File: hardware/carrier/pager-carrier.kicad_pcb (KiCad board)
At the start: 2 copper layers, 46.2 x 51 mm, 80 parts, among them J1 PANEL, J2 CARDKB, J3 HAPTIC, J4 EXT_LED, J5 PIEZ, J6 USB4235, J7 BATTERY, J8 FRONTLIGHT, M1 Walter, Q1 UMH3N, Q2 SI1308EDL, Q3 MMST3904, Q4 AO3401A, SW1 KMR221GLFS, SW2 JS102011SAQN, U1 CP2102N-A02-GQFN24, U2 SN74LVC2G126DCUR, U3 DRV2605LDGSR, U4 LIS2DW12TR, U5 BQ25185DLHR, U6 MAX17048G+T10, U7 TPS62840DLCR

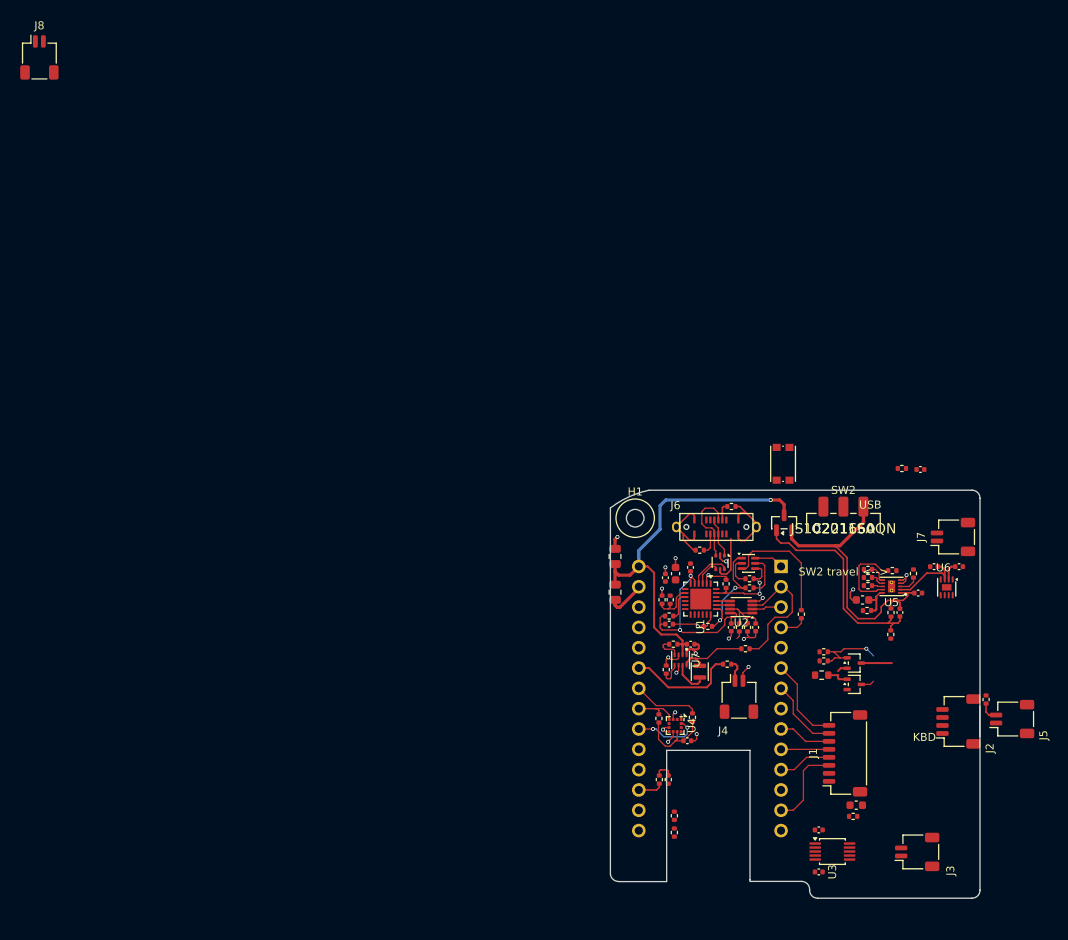
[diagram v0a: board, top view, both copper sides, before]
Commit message: Hand routed the carrier board
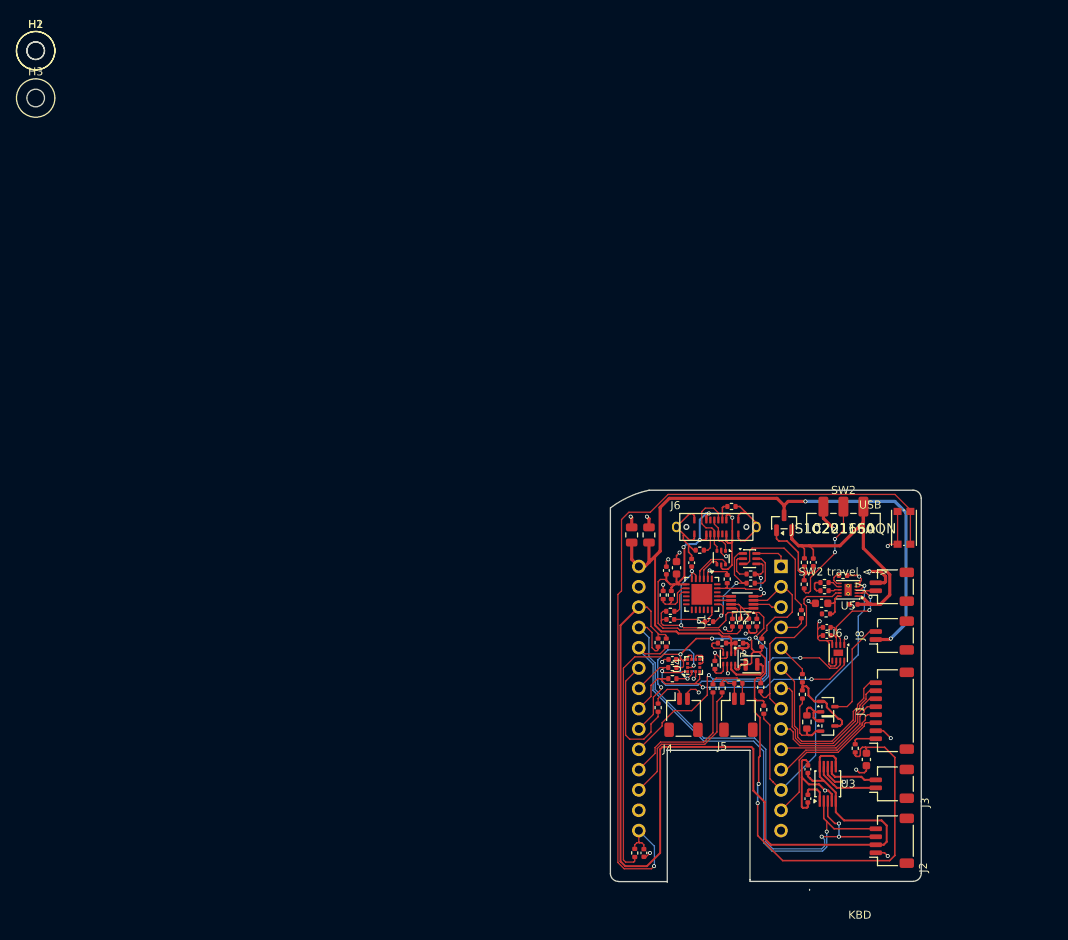
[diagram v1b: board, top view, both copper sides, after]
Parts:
- added H2: Cassette M2, pager-carrier:MountingHole_2.2mm_M2_Cassette, F.Cu at (2.46, 2.46)
- added H3: Cassette M2, pager-carrier:MountingHole_2.2mm_M2_Cassette, F.Cu at (2.46, 8.38)
- moved J8 128.7 mm to (109.5, 75.6), turned to 90 degrees
- moved H1 95.0 mm to (2.46, 2.46)
- moved C5 59.1 mm to (78.5, 102.7), turned to -90 degrees
- moved R5 58.5 mm to (77.3, 102.7), turned to -90 degrees
- moved J5 34.2 mm to (90.3, 85.5), turned to 0 degrees
- moved R20 34.2 mm to (87.1, 82.2), turned to 90 degrees
- moved R28 25.3 mm to (93.5, 84.8)
- moved R16 23.8 mm to (81.3, 76.5)
- moved R26 22.0 mm to (93.1, 82.0), turned to -90 degrees
- moved R15 21.7 mm to (80.3, 76.5)
- moved C17 18.2 mm to (101.3, 74.5), turned to 180 degrees
- moved SW1 17.1 mm to (111.0, 62.1), turned to -90 degrees
- moved J2 17.1 mm to (109.5, 101.2)
- moved C16 15.9 mm to (101.3, 75.6)
- moved U6 15.8 mm to (102.8, 77.7)
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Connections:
- net Net-(Q4-G) renamed /Power/SYS_GATE
- U3 pad 7: Net-(J3-Pin_1) -> Net-(J3-Pin_2)
- U3 pad 9: Net-(J3-Pin_2) -> Net-(J3-Pin_1)
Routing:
- net 3V3_AWK: track 0.00 -> 120.6 mm
- net 3V3: track 19.2 -> 128.5 mm, vias 0 -> 6
- net /Core/FL_BTN: track 0.00 -> 99.8 mm, vias 0 -> 1
- net /Core/AWK_SDA: track 0.00 -> 63.5 mm, vias 0 -> 3
- net GND: track 66.0 -> 125.8 mm, vias 20 -> 30
- net /Core/AWK_SCL: track 0.00 -> 59.6 mm, vias 0 -> 1
- net VBUS: track 6.90 -> 51.3 mm, vias 0 -> 4
- net SYS_SW: track 48.6 -> 88.9 mm, vias 1 -> 2
- net CHG_STAT2: track 2.17 -> 41.5 mm, vias 0 -> 1
- net VBUS_DET: track 8.13 -> 40.3 mm, vias 0 -> 2
- net AON_SDA: track 5.76 -> 34.5 mm, vias 0 -> 2
- net AON_SCL: track 8.92 -> 36.5 mm, vias 0 -> 2
- net /Core/PIEZ_N: track 0.00 -> 16.7 mm
- net /Core/PIEZ_P: track 3.16 -> 19.7 mm
- net /Power/SYS_GATE: track 27.2 -> 11.4 mm
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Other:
- board size 46.2 x 51 mm -> 38.9 x 50 mm
